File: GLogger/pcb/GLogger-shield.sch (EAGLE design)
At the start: 10 parts, among them IC2 RV_3049_C2

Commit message: ADXL345 and SC-Card.
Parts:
- removed JP2: (no value), pinhead:PINHD-1X8/90
- added ADXL345-JP1, ADXL345-JP2: (no value), pinhead:PINHD-1X5
- added JP1: (no value), pinhead:PINHD-1X6
- added SD-CARD: (no value), pinhead:PINHD-2X8
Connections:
- net +3V3: now also JP1.2; no longer JP2.2
- net +5V: now also ADXL345-JP1.1, JP1.1, SD-CARD.5; no longer JP2.1
- net A6: no longer JP2.7
- net A7: no longer JP2.8
- net AD4/SDA: now also ADXL345-JP2.1; no longer IC2.CS
- net AD5/SCL: now also ADXL345-JP2.2
- net GND: now also ADXL345-JP1.2, JP1.3, SD-CARD.1; no longer JP2.3
- net IO0: now also JP1.5; no longer JP2.5
- net IO1: now also JP1.4; no longer JP2.4
- net IO9: now also IC2.CS
- net MISO: now also SD-CARD.13
- net MOSI: now also SD-CARD.9
- net RESET: now also JP1.6; no longer JP2.6
- net SCK: now also SD-CARD.11
- net SS: now also SD-CARD.7
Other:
- note removed: "Achtung! -------------------------------------------------- Verbindung AD4 zu LCD-Reset trennen und auf Reset des Arduino legen. AD3 zu LCD-CS ggf. trennen und auf VCC legen."
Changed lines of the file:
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@@
 <part name="P+2" library="supply1" deviceset="+5V" device=""/>
 <part name="U$1" library="SparkFun-Boards" deviceset="ARDUINO_PRO_MINI" device=""/>
-<part name="JP2" library="pinhead" deviceset="PINHD-1X8" device="/90"/>
+<part name="SD-CARD" library="pinhead" deviceset="PINHD-2X8" device=""/>
+<part name="ADXL345-JP1" library="pinhead" deviceset="PINHD-1X5" device=""/>
+<part name="ADXL345-JP2" library="pinhead" deviceset="PINHD-1X5" device=""/>
+<part name="JP1" library="pinhead" deviceset="PINHD-1X6" device=""/>
 </parts>
 <sheets>
@@
 <text x="332.74" y="149.86" size="1.778" layer="91">SCL</text>
 <text x="309.88" y="27.94" size="2.54" layer="95">TINO Shield</text>
-<text x="337.82" y="101.6" size="1.778" layer="91">Achtung!
---------------------------------------------------
-Verbindung AD4 zu LCD-Reset trennen
-und auf Reset des Arduino legen.
-AD3 zu LCD-CS ggf. trennen und
-auf VCC legen.</text>
 </plain>
 <instances>
@@
 </instance>
 <instance part="U$1" gate="G$1" x="251.46" y="198.12"/>
-<instance part="JP2" gate="A" x="330.2" y="231.14"/>
+<instance part="SD-CARD" gate="A" x="129.54" y="139.7"/>
+<instance part="ADXL345-JP1" gate="A" x="119.38" y="93.98"/>
+<instance part="ADXL345-JP2" gate="A" x="144.78" y="93.98"/>
+<instance part="JP1" gate="A" x="330.2" y="233.68"/>
 </instances>
 <busses>
@@
 <wire x1="327.66" y1="241.3" x2="307.34" y2="241.3" width="0.1524" layer="91"/>
 <label x="307.34" y="241.3" size="1.778" layer="95"/>
-<pinref part="JP2" gate="A" pin="1"/>
+<pinref part="JP1" gate="A" pin="1"/>
 </segment>
 <segment>
@@
 <junction x="152.4" y="218.44"/>
 <pinref part="P+2" gate="1" pin="+5V"/>
+</segment>
+<segment>
+<pinref part="SD-CARD" gate="A" pin="5"/>
+<wire x1="127" y1="142.24" x2="109.22" y2="142.24" width="0.1524" layer="91"/>
+<label x="109.22" y="142.24" size="1.778" layer="95"/>
+</segment>
+<segment>
+<pinref part="ADXL345-JP1" gate="A" pin="1"/>
+<wire x1="116.84" y1="99.06" x2="99.06" y2="99.06" width="0.1524" layer="91"/>
+<label x="99.06" y="99.06" size="1.778" layer="95"/>
 </segment>
 </net>
@@
 <wire x1="327.66" y1="236.22" x2="307.34" y2="236.22" width="0.1524" layer="91"/>
 <label x="307.34" y="236.22" size="1.778" layer="95"/>
-<pinref part="JP2" gate="A" pin="3"/>
+<pinref part="JP1" gate="A" pin="3"/>
 </segment>
 <segment>
@@
 <wire x1="165.1" y1="190.5" x2="165.1" y2="185.42" width="0.1524" layer="91"/>
 </segment>
+<segment>
+<pinref part="SD-CARD" gate="A" pin="1"/>
+<wire x1="127" y1="147.32" x2="109.22" y2="147.32" width="0.1524" layer="91"/>
+<label x="109.22" y="147.32" size="1.778" layer="95"/>
+</segment>
+<segment>
+<pinref part="ADXL345-JP1" gate="A" pin="2"/>
+<wire x1="116.84" y1="96.52" x2="99.06" y2="96.52" width="0.1524" layer="91"/>
+<label x="99.06" y="96.52" size="1.778" layer="95"/>
+</segment>
 </net>
 <net name="AREF" class="4">
@@
 <label x="86.36" y="193.04" size="1.27" layer="95" rot="R180" xref="yes"/>
 </segment>
+<segment>
+<pinref part="SD-CARD" gate="A" pin="11"/>
+<wire x1="127" y1="134.62" x2="109.22" y2="134.62" width="0.1524" layer="91"/>
+<label x="109.22" y="134.62" size="1.778" layer="95"/>
+</segment>
 </net>
 <net name="+3V3" class="0">
@@
 <wire x1="327.66" y1="238.76" x2="307.34" y2="238.76" width="0.1524" layer="91"/>
 <label x="307.34" y="238.76" size="1.778" layer="95"/>
-<pinref part="JP2" gate="A" pin="2"/>
+<pinref part="JP1" gate="A" pin="2"/>
 </segment>
 </net>
@@
 <label x="86.36" y="187.96" size="1.27" layer="95" rot="R180" xref="yes"/>
 </segment>
+<segment>
+<pinref part="SD-CARD" gate="A" pin="13"/>
+<wire x1="127" y1="132.08" x2="109.22" y2="132.08" width="0.1524" layer="91"/>
+<label x="109.22" y="132.08" size="1.778" layer="95"/>
+</segment>
 </net>
 <net name="MOSI" class="0">
@@
 <label x="86.36" y="182.88" size="1.27" layer="95" rot="R180" xref="yes"/>
 </segment>
+<segment>
+<pinref part="SD-CARD" gate="A" pin="9"/>
+<wire x1="127" y1="137.16" x2="109.22" y2="137.16" width="0.1524" layer="91"/>
+<label x="109.22" y="137.16" size="1.778" layer="95"/>
+</segment>
 </net>
 <net name="SS" class="0">
@@
 <pinref part="U$1" gate="G$1" pin="*10"/>
 </segment>
+<segment>
+<pinref part="SD-CARD" gate="A" pin="7"/>
+<wire x1="127" y1="139.7" x2="109.22" y2="139.7" width="0.1524" layer="91"/>
+<label x="109.22" y="139.7" size="1.778" layer="95"/>
+</segment>
 </net>
 <net name="AD0" class="0">
@@
 </segment>
 <segment>
-<wire x1="111.76" y1="198.12" x2="86.36" y2="198.12" width="0.1524" layer="91"/>
-<label x="86.36" y="198.12" size="1.27" layer="95" rot="R180" xref="yes"/>
-<pinref part="IC2" gate="A" pin="CS"/>
+<pinref part="ADXL345-JP2" gate="A" pin="1"/>
+<wire x1="142.24" y1="99.06" x2="127" y2="99.06" width="0.1524" layer="91"/>
+<label x="127" y="99.06" size="1.778" layer="95"/>
 </segment>
 </net>
@@
 <label x="218.44" y="177.8" size="1.778" layer="95"/>
 <pinref part="U$1" gate="G$1" pin="A5"/>
+</segment>
+<segment>
+<pinref part="ADXL345-JP2" gate="A" pin="2"/>
+<wire x1="142.24" y1="96.52" x2="127" y2="96.52" width="0.1524" layer="91"/>
+<label x="127" y="96.52" size="1.778" layer="95"/>
 </segment>
 </net>
@@
 <wire x1="307.34" y1="233.68" x2="327.66" y2="233.68" width="0.1524" layer="91"/>
 <label x="307.34" y="233.68" size="1.778" layer="95"/>
-<pinref part="JP2" gate="A" pin="4"/>
+<pinref part="JP1" gate="A" pin="4"/>
 </segment>
 </net>
@@
 <wire x1="327.66" y1="231.14" x2="307.34" y2="231.14" width="0.1524" layer="91"/>
 <label x="307.34" y="231.14" size="1.778" layer="95"/>
-<pinref part="JP2" gate="A" pin="5"/>
+<pinref part="JP1" gate="A" pin="5"/>
 </segment>
 </net>
@@
 <label x="218.44" y="185.42" size="1.778" layer="95"/>
 <pinref part="U$1" gate="G$1" pin="*9"/>
+</segment>
+<segment>
+<wire x1="111.76" y1="198.12" x2="86.36" y2="198.12" width="0.1524" layer="91"/>
+<label x="86.36" y="198.12" size="1.27" layer="95" rot="R180" xref="yes"/>
+<pinref part="IC2" gate="A" pin="CS"/>
 </segment>
 </net>
@@
 <wire x1="327.66" y1="228.6" x2="307.34" y2="228.6" width="0.1524" layer="91"/>
 <label x="307.34" y="228.6" size="1.778" layer="95"/>
-<pinref part="JP2" gate="A" pin="6"/>
+<pinref part="JP1" gate="A" pin="6"/>
 </segment>
 </net>
 <net name="A6" class="0">
 <segment>
-<wire x1="327.66" y1="226.06" x2="307.34" y2="226.06" width="0.1524" layer="91"/>
-<label x="307.34" y="226.06" size="1.778" layer="95"/>
 <wire x1="289.56" y1="177.8" x2="264.16" y2="177.8" width="0.1524" layer="91"/>
 <label x="281.94" y="177.8" size="1.778" layer="95"/>
 <pinref part="U$1" gate="G$1" pin="A6"/>
-<pinref part="JP2" gate="A" pin="7"/>
 </segment>
 </net>
 <net name="A7" class="0">
 <segment>
-<wire x1="327.66" y1="223.52" x2="307.34" y2="223.52" width="0.1524" layer="91"/>
-<label x="307.34" y="223.52" size="1.778" layer="95"/>
 <wire x1="289.56" y1="180.34" x2="264.16" y2="180.34" width="0.1524" layer="91"/>
 <label x="281.94" y="180.34" size="1.778" layer="95"/>
 <pinref part="U$1" gate="G$1" pin="A7"/>
-<pinref part="JP2" gate="A" pin="8"/>
 </segment>
 </net>
@@
 </schematic>
 </drawing>
-<compatibility>
-<note version="6.3" minversion="6.2.2" severity="warning">
-Since Version 6.2.2 text objects can contain more than one line,
-which will not be processed correctly with this version.
-</note>
-</compatibility>
 </eagle>

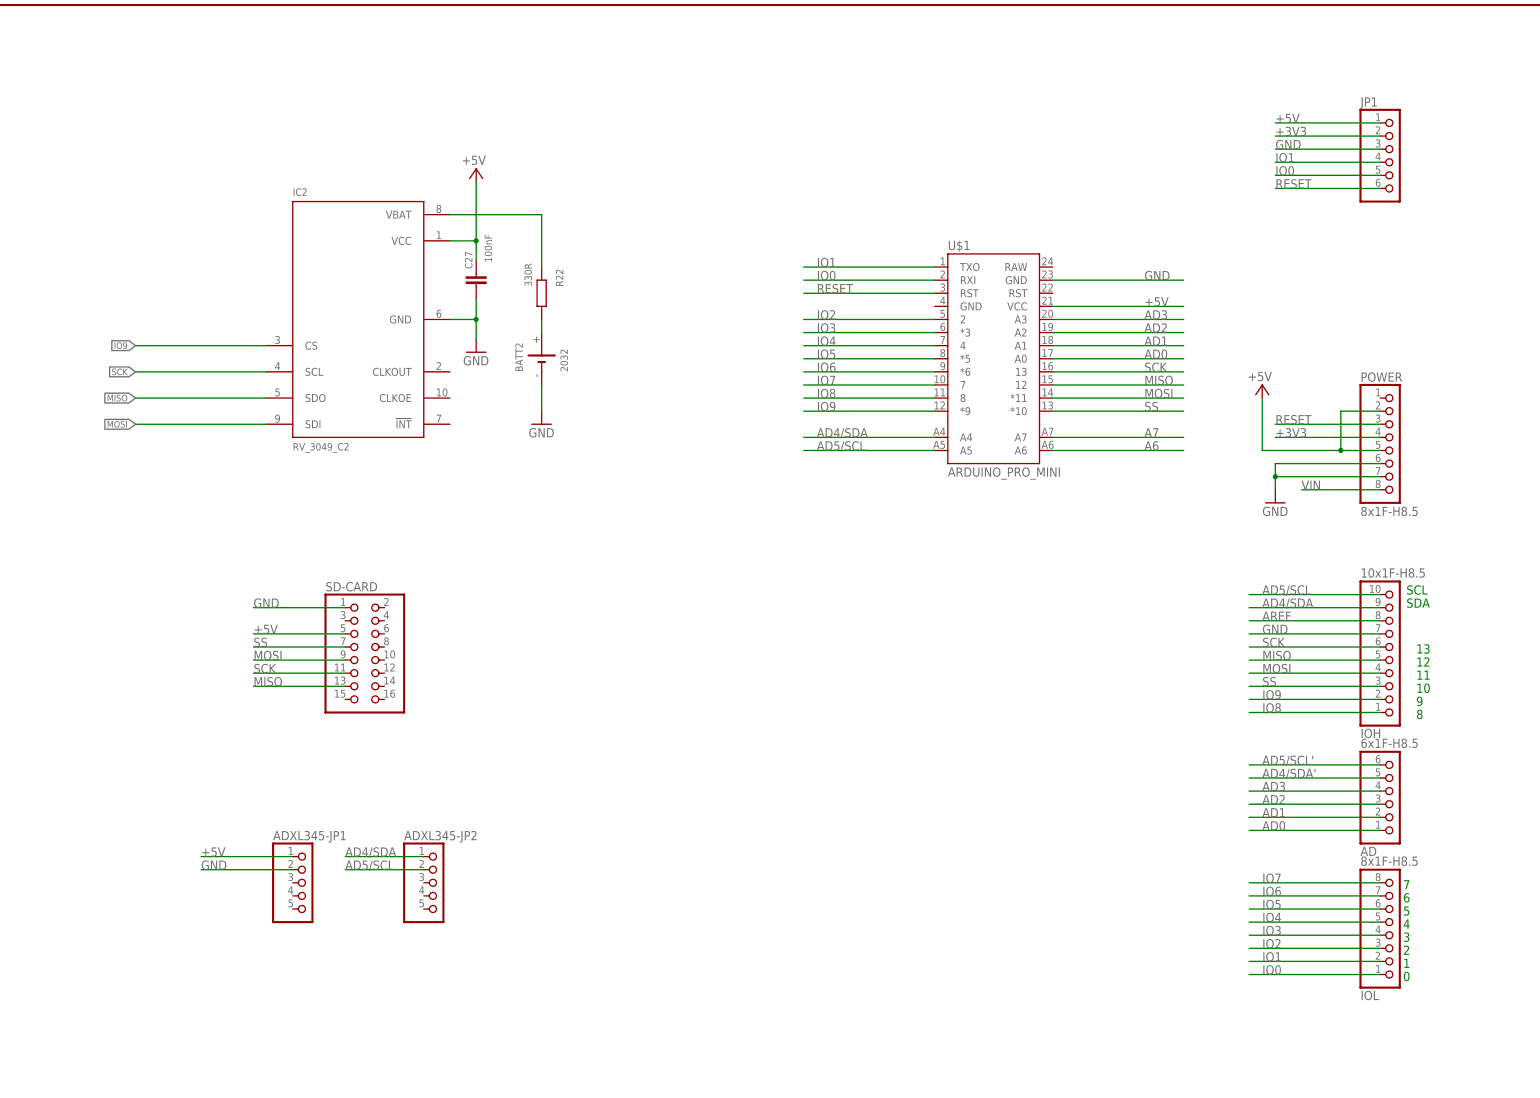
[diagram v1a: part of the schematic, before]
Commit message: switch to fat16.
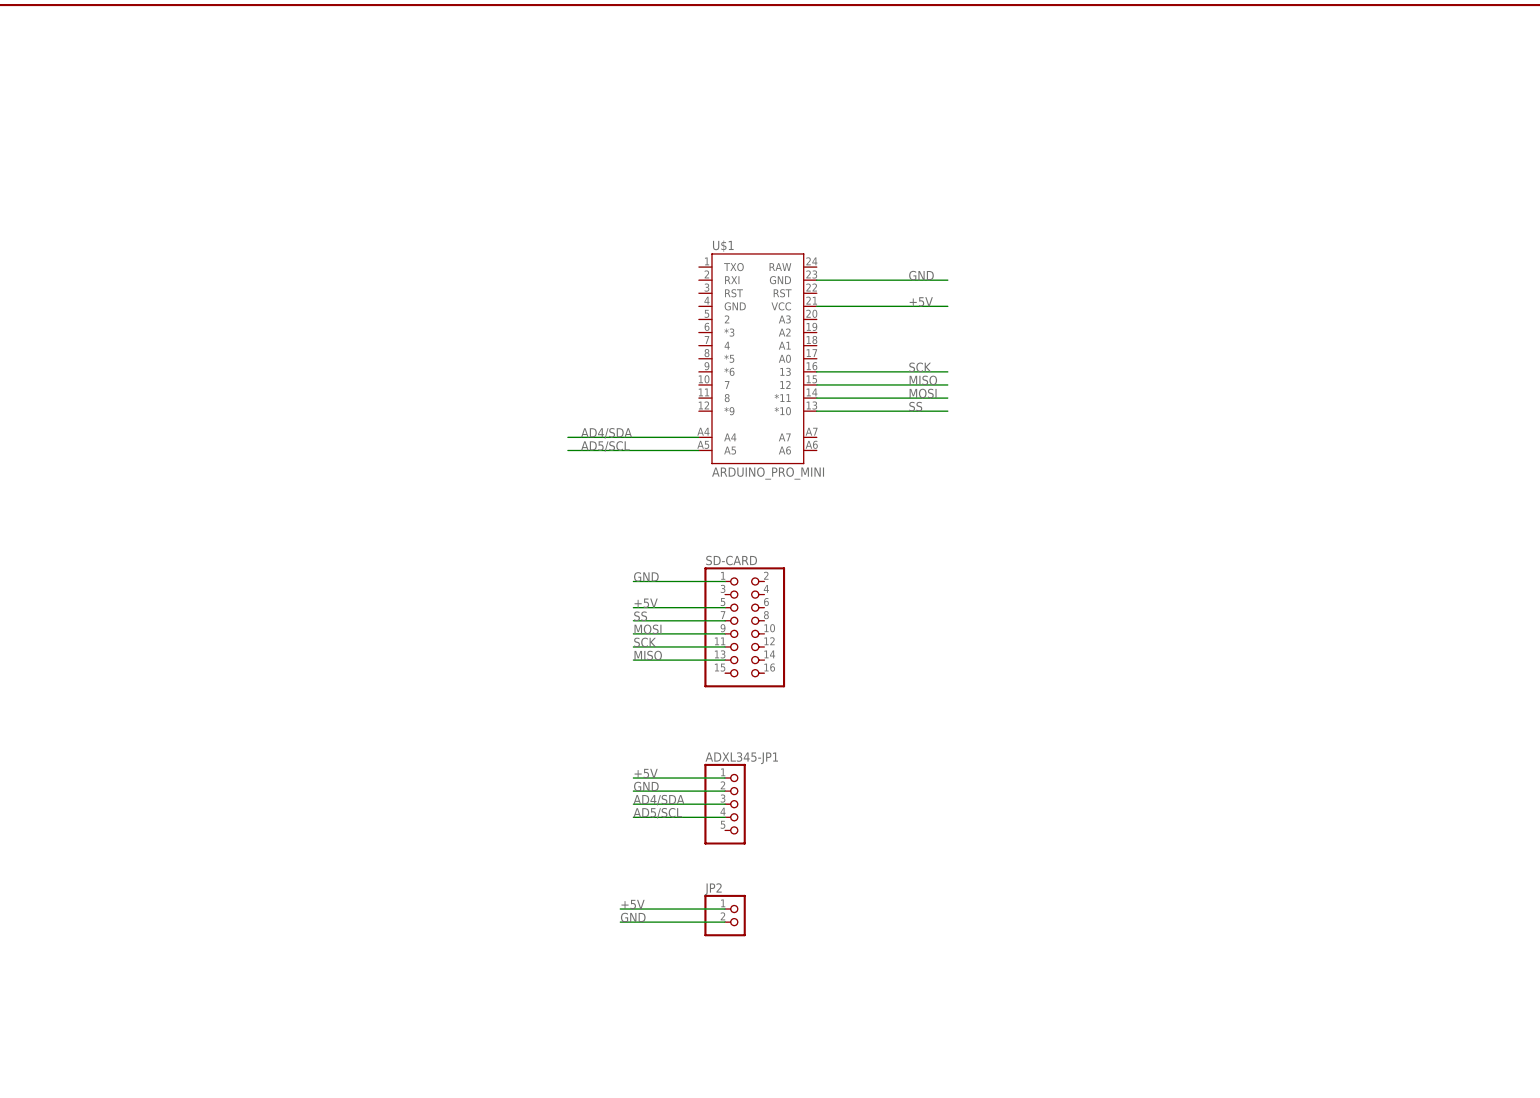
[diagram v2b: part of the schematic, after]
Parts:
- removed AD: 6x1F-H8.5, SmartPrj:PINHD-1X6
- removed ADXL345-JP2: (no value), pinhead:PINHD-1X5
- removed BATT2: 2032, El_Mech:CR2032_HOLDSMD
- removed C27: 100nF, rcl:C-EUC0603
- removed IC2: RV_3049_C2, RTC_Quarz:RV_3049_C2
- removed IOH: 10x1F-H8.5, SmartPrj:PINHD-1X10_ARD
- removed IOL, POWER: 8x1F-H8.5, SmartPrj:PINHD-1X8
- removed JP1: (no value), pinhead:PINHD-1X6
- removed R22: 330R, rcl:R-EU_R0603
- added JP2: (no value), pinhead:PINHD-1X2
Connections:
- removed net +3V3: JP1.2, POWER.4
- removed net +BAT: BATT2.+, R22.1
- removed net A6: U$1.A6
- removed net A7: U$1.A7
- removed net AD0: AD.1, U$1.A0
- removed net AD1: AD.2, U$1.A1
- removed net AD2: AD.3, U$1.A2
- removed net AD3: AD.4, U$1.A3
- removed net AD4/SDA': AD.5
- removed net AD5/SCL': AD.6
- removed net AREF: IOH.8
- removed net IO0: IOL.1, JP1.5, U$1.RXI
- removed net IO1: IOL.2, JP1.4, U$1.TXO
- removed net IO2: IOL.3, U$1.2
- removed net IO3: IOL.4, U$1.*3
- removed net IO4: IOL.5, U$1.4
- removed net IO5: IOL.6, U$1.*5
- removed net IO6: IOL.7, U$1.*6
- removed net IO7: IOL.8, U$1.7
- removed net IO8: IOH.1, U$1.8
- removed net IO9: IC2.CS, IOH.2, U$1.*9
- removed net N$25: IC2.VBAT, R22.2
- removed net RESET: JP1.6, POWER.3, U$1.RST
- removed net VIN: POWER.8
- net +5V: now also JP2.1; no longer C27.1, IC2.VCC, JP1.1, POWER.2, POWER.5
- net AD4/SDA: now also ADXL345-JP1.3; no longer ADXL345-JP2.1, IOH.9
- net AD5/SCL: now also ADXL345-JP1.4; no longer ADXL345-JP2.2, IOH.10
- net GND: now also JP2.2; no longer BATT2.-, C27.2, IC2.GND, IOH.7, JP1.3, POWER.6, POWER.7
- net MISO: no longer IC2.SDO, IOH.5
- net MOSI: no longer IC2.SDI, IOH.4
- net SCK: no longer IC2.SCL, IOH.6
- net SS: no longer IOH.3
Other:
- note removed: "0"
- note removed: "1"
- note removed: "10"
- note removed: "11"
- note removed: "12"
- note removed: "13"
- note removed: "2"
- note removed: "3"
- note removed: "4"
- note removed: "5"
- note removed: "6"
- note removed: "7"
- note removed: "8"
- note removed: "9"
- note removed: "SCL"
- note removed: "SDA"
- moved on the sheet: ADXL345-JP1, SD-CARD, U$1

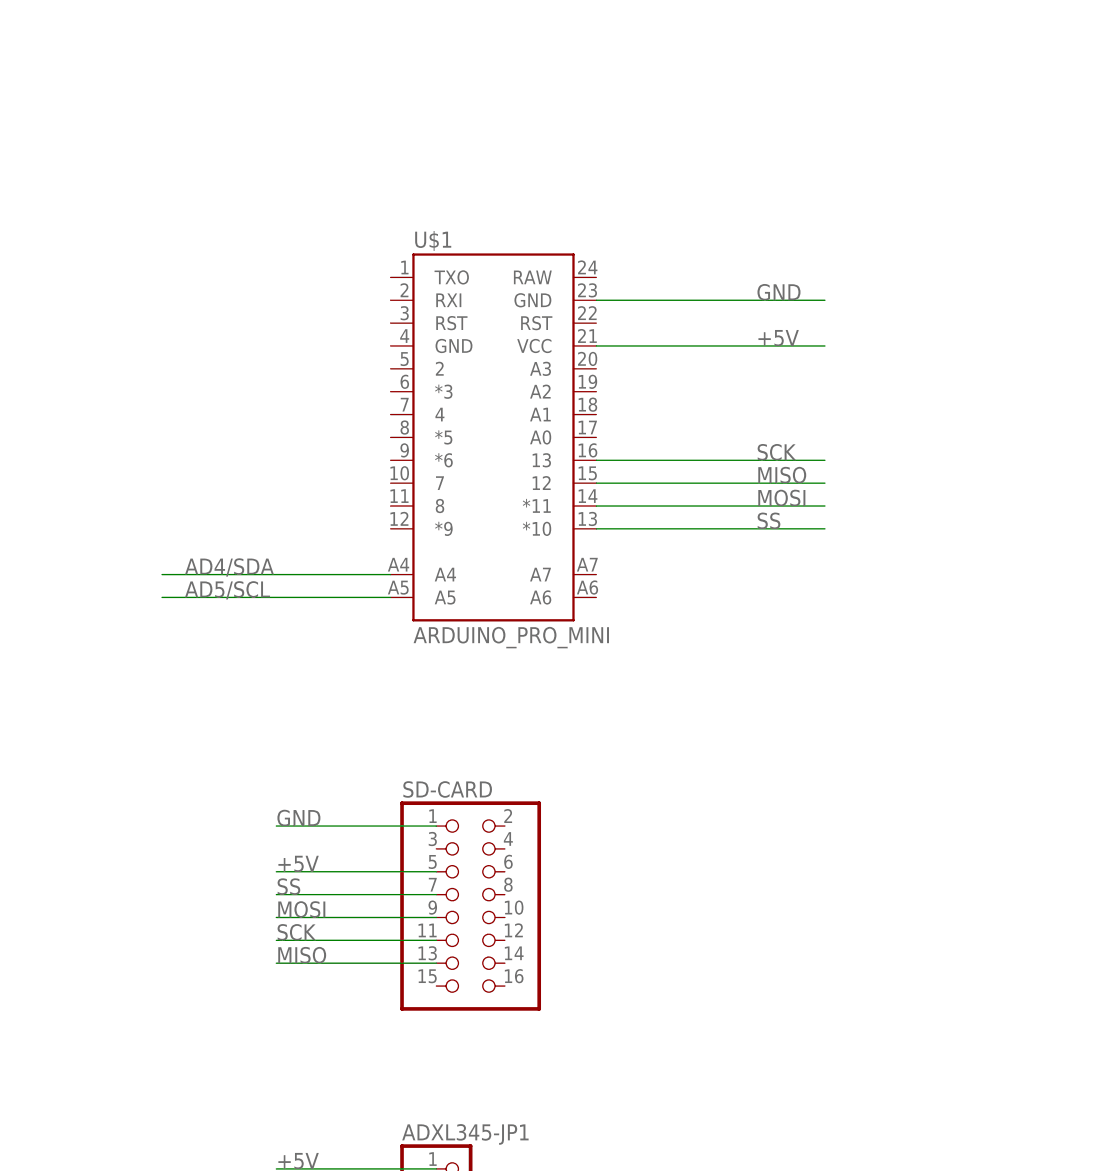
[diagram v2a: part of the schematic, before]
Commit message: new Layout.
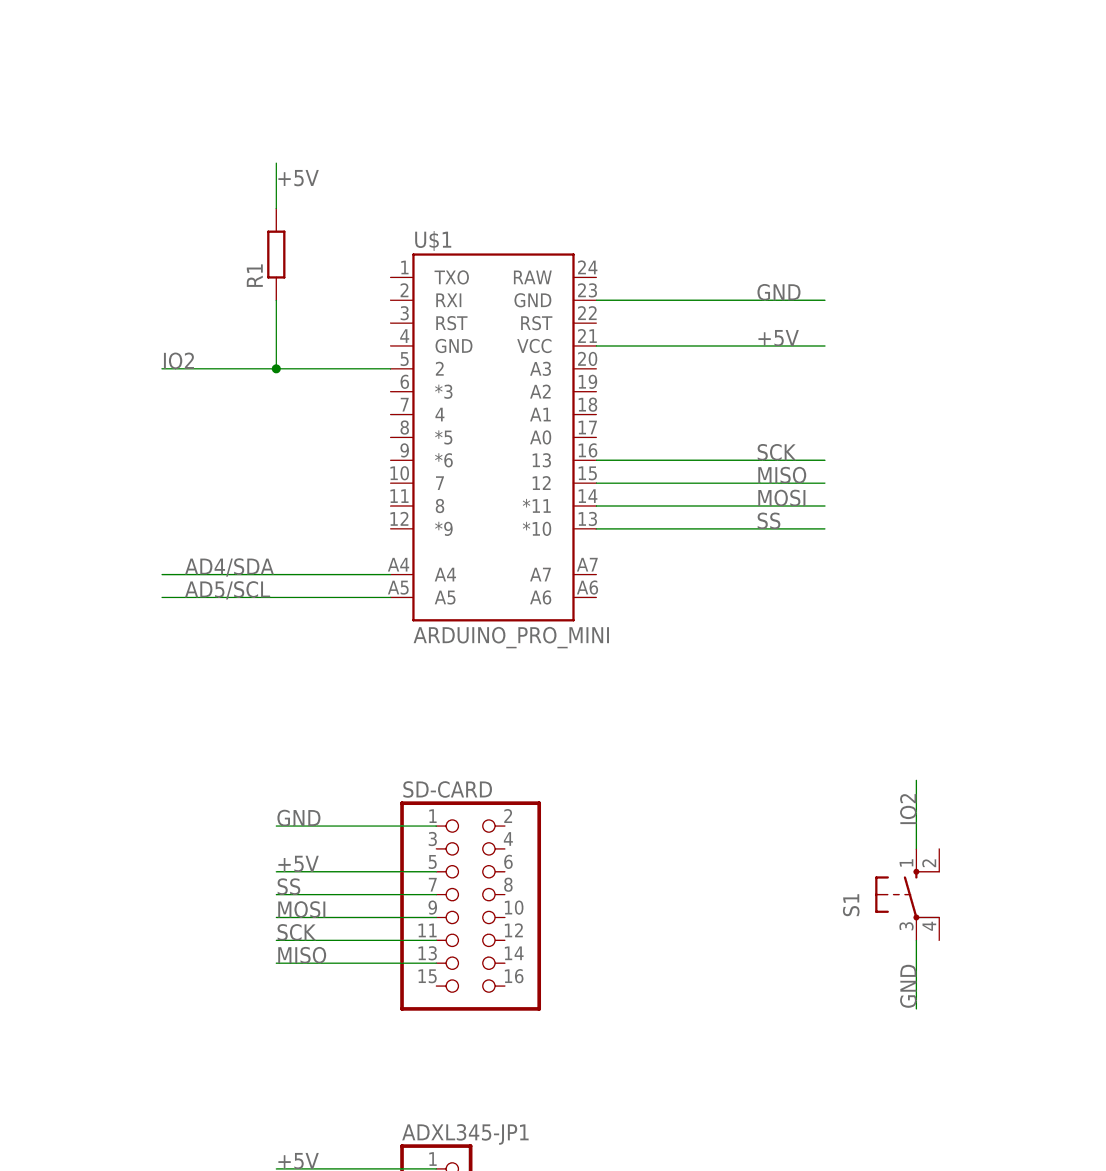
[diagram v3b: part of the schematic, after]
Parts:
- added R1: (no value), resistor:R-EU_0207/10
- added S1: (no value), arduino_adafruit:40-XX-ROUND
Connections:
- new net IO2: R1.1, S1.S, U$1.2
- net +5V: now also R1.2
- net GND: now also S1.P
